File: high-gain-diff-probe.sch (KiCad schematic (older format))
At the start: 51 parts

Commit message: Transformer driver?
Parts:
- added C13, C14, C? (x2): 100nF, symbol Device:C_Small
- added C? (x6): C, symbol Device:C
- added C? (x6): 47uF, symbol Device:CP1
- added D? (x4): D_Schottky, symbol Device:D_Schottky
- added J?: Barrel_Jack, symbol Connector:Barrel_Jack
- added L? (x2): 33uH, symbol Device:L
- added R?: 10k, symbol Device:R_US
- added T?: Transformer_SP_2S, symbol Device:Transformer_SP_2S
- added U?: L7815, symbol Regulator_Linear:L7815
- added U?: L7915, symbol Regulator_Linear:L7915
- added U?: SN6505ADBV, Package_TO_SOT_SMD:SOT-23-6, symbol Power_Management:SN6505ADBV
- added U?: LT3439, Package_SO:TSSOP-16-1EP_4.4x5mm_P0.65mm, symbol Regulator_Switching:LT3439
- gave numbers to parts that had none: 49
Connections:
- net labels added: +36V
- wire segments 146 -> 257
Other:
- note added: "TODO: Common\nmode trim"
- note added: "TODO: Gain trim"
- note added: "TODO: Or just 4 9V"
- moved on the sheet: C1, C10, C11, C12, C2, C3, C4, C5, C6, C7, C8, C9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

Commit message: Developing
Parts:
- removed C? (x4): C, symbol Device:C
- removed C? (x5): 47uF, symbol Device:CP1
- removed D? (x4): D_Schottky, symbol Device:D_Schottky
- removed FB1, FB2: Ferrite_Bead, symbol Device:Ferrite_Bead
- removed J?: Barrel_Jack, symbol Connector:Barrel_Jack
- removed L? (x2): 33uH, symbol Device:L
- removed R10: 6k, symbol Device:R_US
- removed R16, R18: 100, symbol Device:R_US
- removed R8: 316, symbol Device:R_US
- removed R?: 10k, symbol Device:R_US
- removed SW2: SW_Rotary2x6, symbol Switch:SW_Rotary2x6
- removed SW3: LOW PASS SELECT, symbol Switch:SW_SP3T
- removed SW4: EXTRA GAIN SELECT, symbol Switch:SW_SP3T
- removed T?: Transformer_SP_2S, symbol Device:Transformer_SP_2S
- removed U2: ADA4004-2, symbol Amplifier_Operational:ADA4075-2
- removed U3: ADA4000-2, symbol Amplifier_Operational:ADA4075-2
- removed U?: L7815, symbol Regulator_Linear:L7815
- removed U?: L7915, symbol Regulator_Linear:L7915
- removed U?: SN6505ADBV, Package_TO_SOT_SMD:SOT-23-6, symbol Power_Management:SN6505ADBV
- removed U?: LT3439, Package_SO:TSSOP-16-1EP_4.4x5mm_P0.65mm, symbol Regulator_Switching:LT3439
- added BT1, BT2, BT3, BT4: 9V, symbol Device:Battery_Cell
- added C21, C22: 100nF, symbol Device:C_Small
- added C24: 47uF, symbol Device:CP1
- added C25: 1uF, symbol Device:C
- added C5, C6: 27pF, symbol Device:C
- added C7, C8: 1-3pF, symbol Device:CTRIM
- added D6: LED, symbol Device:LED
- added D? (x2): 1N4001, Diode_THT:D_DO-41_SOD81_P10.16mm_Horizontal, symbol Diode:1N4001
- added J?: Conn_01x03_Female, symbol Connector:Conn_01x03_Female
- added R5, R6: 475k, symbol Device:R_US
- added RV1: 500, symbol Device:R_POT_US
- added SW2: ‎MRB24B‎, symbol Switch:SW_DP3T
- added SW3: SW_SPDT, symbol Switch:SW_SPDT
- added SW4: SW_DPST_x2, symbol Switch:SW_DPST_x2
- added SW5: SW_DP3T, symbol Switch:SW_DPST_x2
- added U2: ADA4004, Package_SO:SOIC-8_3.9x4.9mm_P1.27mm, symbol Amplifier_Operational:LMH6609MA
- added U3: BUF634A, Package_SO:SOIC-8-1EP_3.9x4.9mm_P1.27mm_EP2.41x3.81mm_ThermalVias, symbol high-gain-diff-probe:BUF634A
- C1: value 14pF -> 27pF
- C11: renamed from C7; value 12p -> 10p
- C12: renamed from C8; value 12p -> 10p
- C18: renamed from C10; value 33nF -> 120pF
- C2: renamed from C3; value 14pF -> 27pF
- C20: renamed from C12; value 330nF -> 33nF
- C26: renamed from C?; value C -> 1uF
- C27: renamed from C?; value C -> 100nF
- R1: value 950k -> 475k
- R14, R15: value 2.2k -> 10k
- R17: value 400 -> 15k
- R2: renamed from R3; value 950k -> 475k
- R7: renamed from R6; value 50k -> 47.5k
- R8: renamed from R5; value 50k -> 47.5k
- SW1: value SW_DP3T -> ‎MRB24B‎
- gave numbers to parts that had none: 3
- renumbered C6 to C10, C9 to C13, C13 to C16, C14 to C17, C11 to C19, C2 to C3, C5 to C9, R9 to R10, R19 to R16, R2 to R3, R7 to R9, RV1 to RV2
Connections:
- net labels removed: +36V, RG_1000X, RG_100X
- wire segments 257 -> 185
- no-connect marks 4 -> 3
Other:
- note added: "+-12.8V Offset Range"
- note removed: "TODO: Choose gain switch"
- note removed: "TODO: Common\nmode trim"
- note removed: "TODO: Gain trim"
- note removed: "TODO: LT1010\n"
- note removed: "TODO: Or just 4 9V"
- moved on the sheet: C1, C10, C14, C15, C16, C17, C18, C19, C2, C20, C23, C26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

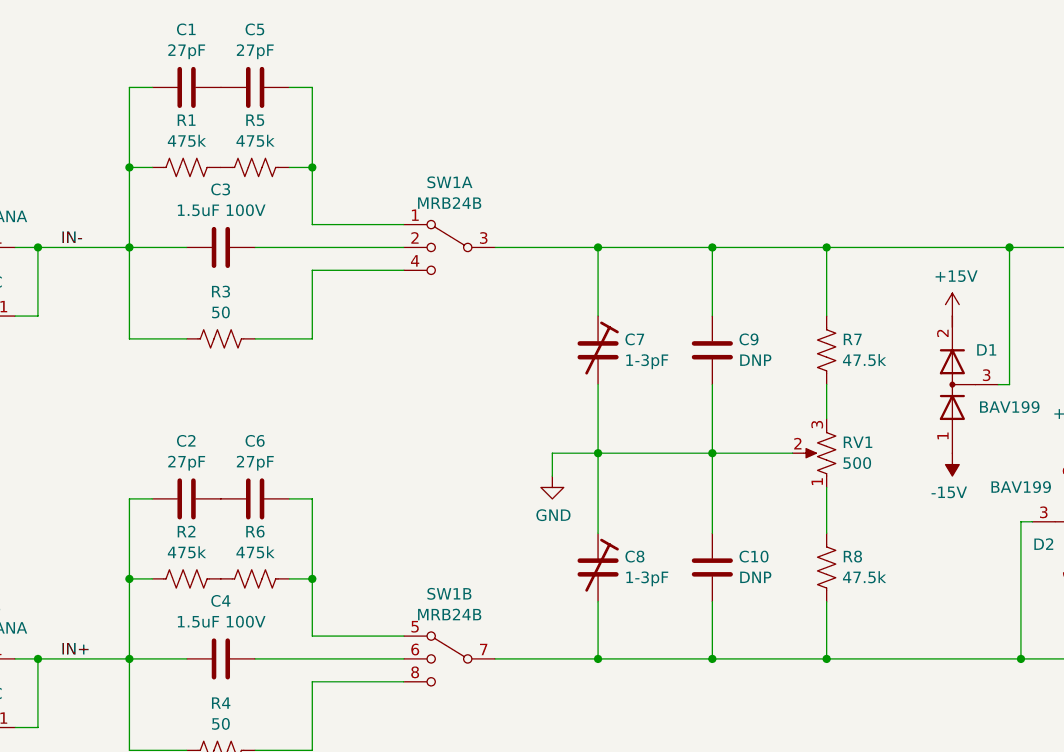
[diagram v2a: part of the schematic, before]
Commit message: Improve input divider ratio
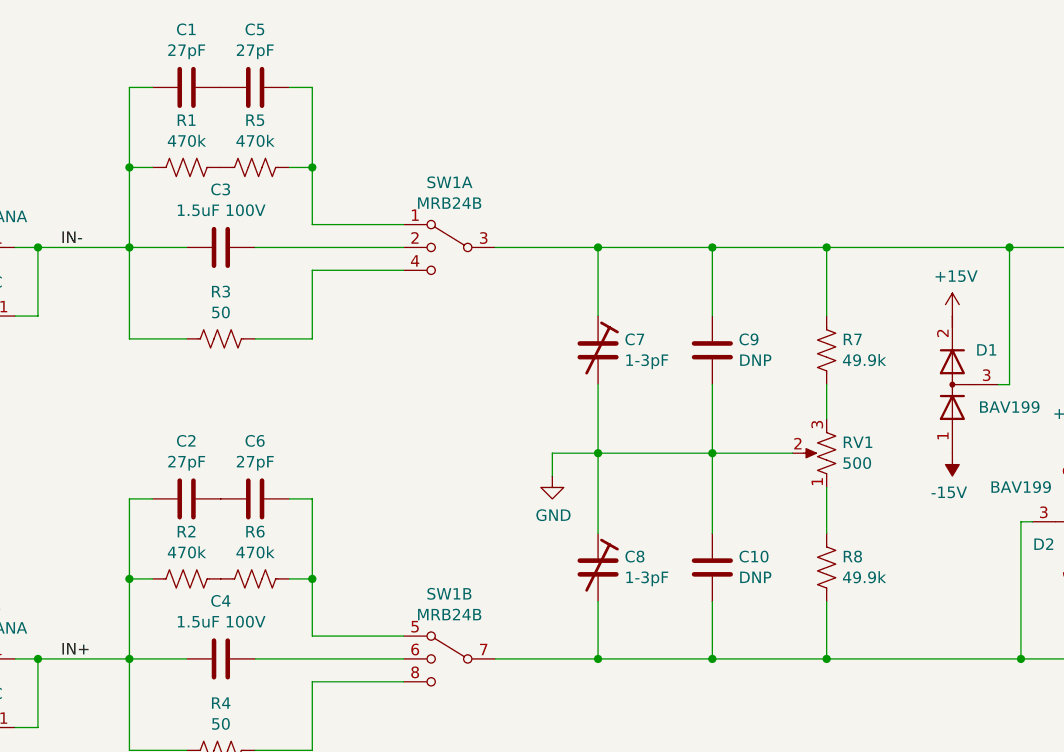
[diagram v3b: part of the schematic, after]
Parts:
- R1, R2, R5, R6: value 475k -> 470k
- R7, R8: value 47.5k -> 49.9k
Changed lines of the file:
@@
 P 5250 2350
 F 0 "R7" H 5318 2396 50  0000 L CNN
-F 1 "47.5k" H 5318 2305 50  0000 L CNN
+F 1 "49.9k" H 5318 2305 50  0000 L CNN
 F 2 "" V 5290 2340 50  0001 C CNN
 F 3 "~" H 5250 2350 50  0001 C CNN
@@
 P 5250 3300
 F 0 "R8" H 5318 3346 50  0000 L CNN
-F 1 "47.5k" H 5318 3255 50  0000 L CNN
+F 1 "49.9k" H 5318 3255 50  0000 L CNN
 F 2 "" V 5290 3290 50  0001 C CNN
 F 3 "~" H 5250 3300 50  0001 C CNN
@@
 P 2450 1550
 F 0 "R1" V 2245 1550 50  0000 C CNN
-F 1 "475k" V 2336 1550 50  0000 C CNN
+F 1 "470k" V 2336 1550 50  0000 C CNN
 F 2 "" V 2490 1540 50  0001 C CNN
 F 3 "~" H 2450 1550 50  0001 C CNN
@@
 P 2450 3350
 F 0 "R2" V 2245 3350 50  0000 C CNN
-F 1 "475k" V 2336 3350 50  0000 C CNN
+F 1 "470k" V 2336 3350 50  0000 C CNN
 F 2 "" V 2490 3340 50  0001 C CNN
 F 3 "~" H 2450 3350 50  0001 C CNN
@@
 Wire Wire Line
 	2200 2300 2450 2300
-Wire Wire Line
-	2750 2300 3000 2300
 $Comp
 L power:GND #PWR08
@@
 P 2750 3350
 F 0 "R6" V 2545 3350 50  0000 C CNN
-F 1 "475k" V 2636 3350 50  0000 C CNN
+F 1 "470k" V 2636 3350 50  0000 C CNN
 F 2 "" V 2790 3340 50  0001 C CNN
 F 3 "~" H 2750 3350 50  0001 C CNN
@@
 P 2750 1550
 F 0 "R5" V 2545 1550 50  0000 C CNN
-F 1 "475k" V 2636 1550 50  0000 C CNN
+F 1 "470k" V 2636 1550 50  0000 C CNN
 F 2 "" V 2790 1540 50  0001 C CNN
 F 3 "~" H 2750 1550 50  0001 C CNN
@@
 	0    1    1    0
 $EndComp
-Wire Wire Line
-	2900 1550 3000 1550
-Wire Wire Line
-	3000 1550 3000 1200
-Wire Wire Line
-	2900 1200 3000 1200
 $Comp
 L Device:C C1
@@
 	3800 1900 4250 1900
 Connection ~ 4250 1900
-Wire Wire Line
-	3000 2300 3000 2000
-Wire Wire Line
-	3000 2000 3400 2000
-Wire Wire Line
-	3400 1800 3000 1800
-Wire Wire Line
-	3000 1800 3000 1550
-Connection ~ 3000 1550
 $Comp
 L Switch:SW_DP3T SW2
@@
 Wire Wire Line
 	4300 8250 4850 8250
+Wire Wire Line
+	3000 2000 3400 2000
+Wire Wire Line
+	2750 2300 3000 2300
+Wire Wire Line
+	3000 2300 3000 2000
+Wire Wire Line
+	2900 1200 3000 1200
+Wire Wire Line
+	3000 1550 3000 1200
+Wire Wire Line
+	2900 1550 3000 1550
+Connection ~ 3000 1550
+Wire Wire Line
+	3400 1800 3000 1800
+Wire Wire Line
+	3000 1800 3000 1550
 $EndSCHEMATC

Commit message: Improve simulations
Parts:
- R1, R2, R5, R6: value 470k -> 475k
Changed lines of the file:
@@
 P 2450 1550
 F 0 "R1" V 2245 1550 50  0000 C CNN
-F 1 "470k" V 2336 1550 50  0000 C CNN
+F 1 "475k" V 2336 1550 50  0000 C CNN
 F 2 "" V 2490 1540 50  0001 C CNN
 F 3 "~" H 2450 1550 50  0001 C CNN
@@
 P 2450 3350
 F 0 "R2" V 2245 3350 50  0000 C CNN
-F 1 "470k" V 2336 3350 50  0000 C CNN
+F 1 "475k" V 2336 3350 50  0000 C CNN
 F 2 "" V 2490 3340 50  0001 C CNN
 F 3 "~" H 2450 3350 50  0001 C CNN
@@
 P 2750 3350
 F 0 "R6" V 2545 3350 50  0000 C CNN
-F 1 "470k" V 2636 3350 50  0000 C CNN
+F 1 "475k" V 2636 3350 50  0000 C CNN
 F 2 "" V 2790 3340 50  0001 C CNN
 F 3 "~" H 2750 3350 50  0001 C CNN
@@
 P 2750 1550
 F 0 "R5" V 2545 1550 50  0000 C CNN
-F 1 "470k" V 2636 1550 50  0000 C CNN
+F 1 "475k" V 2636 1550 50  0000 C CNN
 F 2 "" V 2790 1540 50  0001 C CNN
 F 3 "~" H 2750 1550 50  0001 C CNN

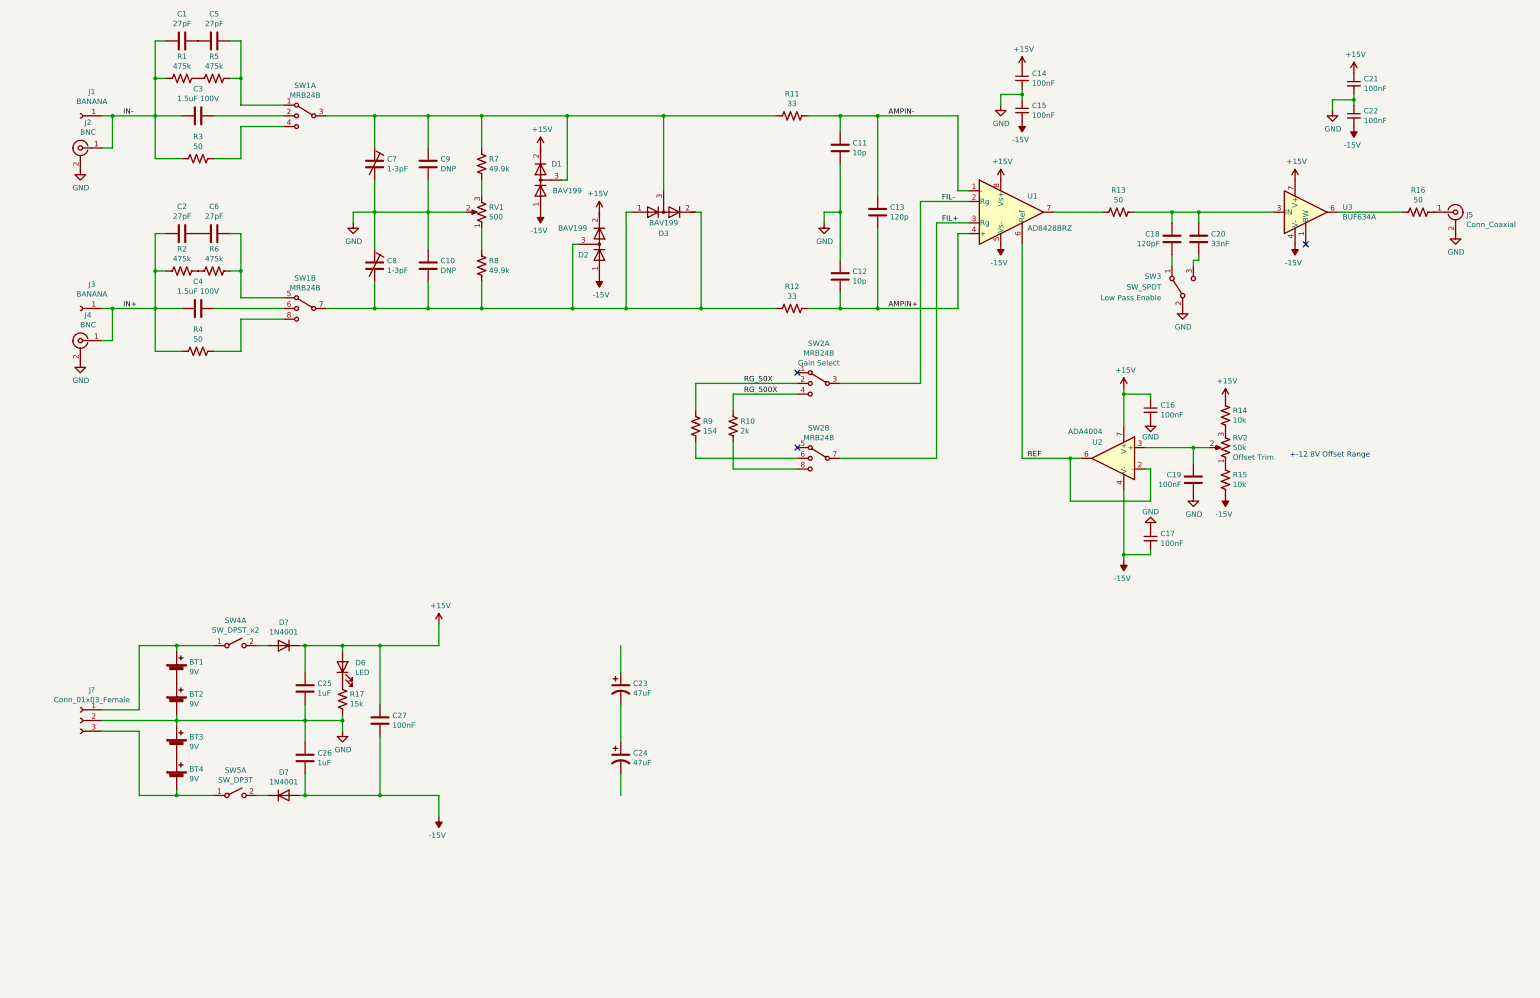
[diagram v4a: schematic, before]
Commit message: Implement capacitance multiplier, power overvoltage protection, and signal out of range comparators
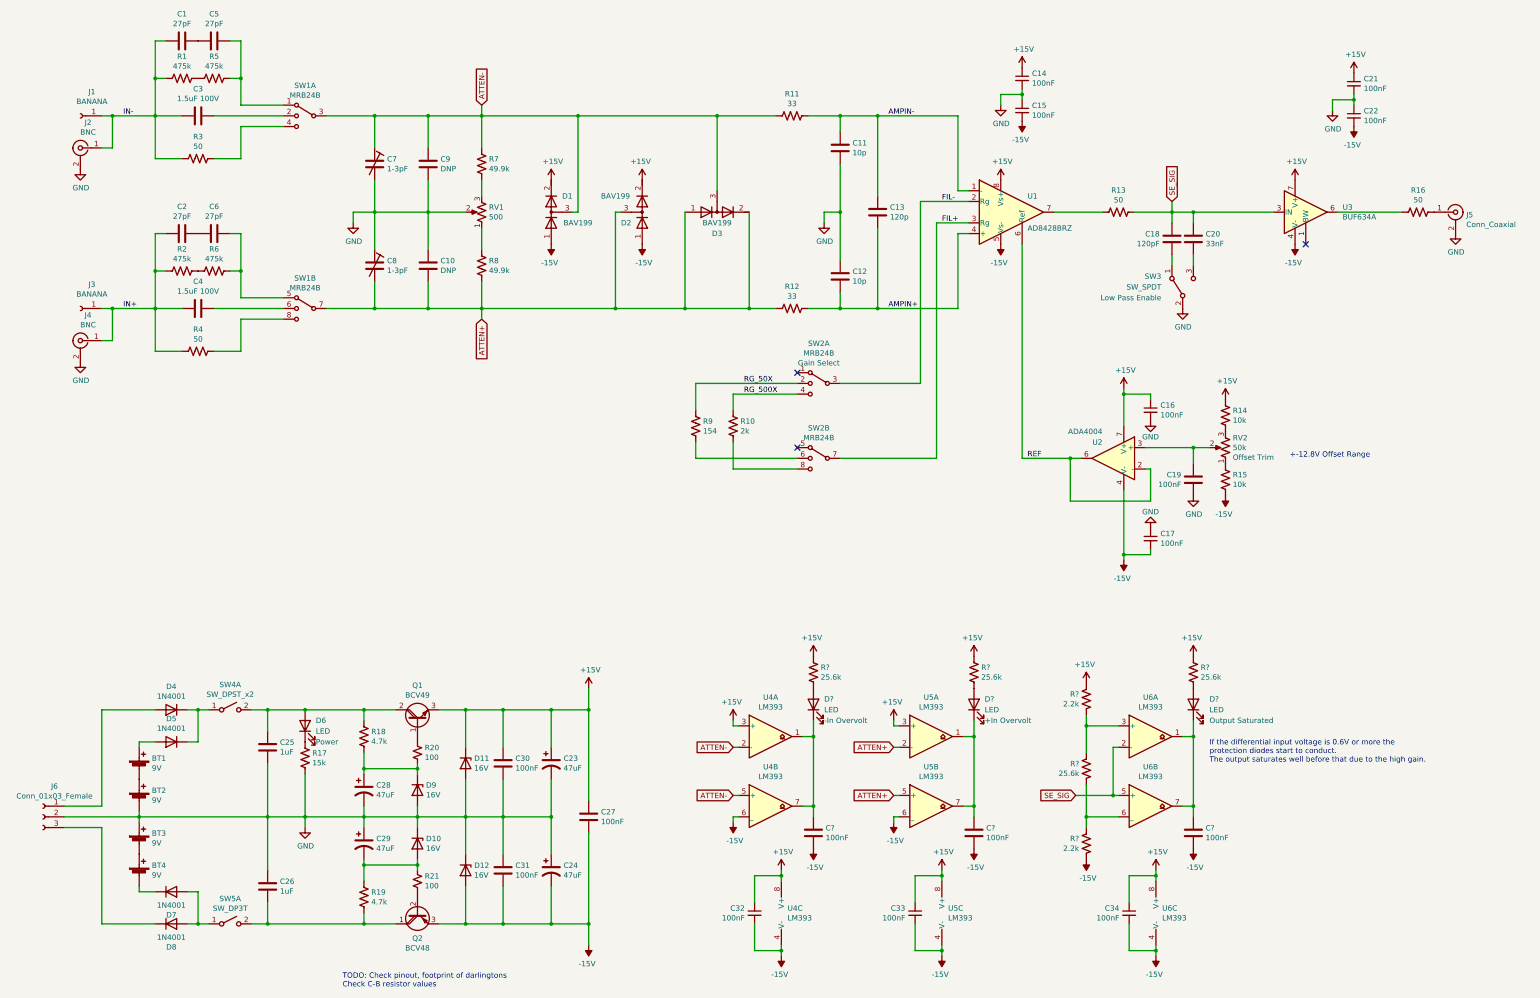
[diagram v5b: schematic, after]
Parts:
- added C28, C29: 47uF, symbol Device:CP1
- added C30, C31, C? (x3): 100nF, symbol Device:C
- added C32, C33, C34: 100nF, symbol Device:C_Small
- added D10, D11, D12, D9: 16V, Diode_SMD:D_SMF, symbol Diode:BZD27Cxx
- added D4, D8: 1N4001, Diode_THT:D_DO-41_SOD81_P10.16mm_Horizontal, symbol Diode:1N4001
- added D? (x3): LED, symbol Device:LED
- added Q1: BCV49, Package_TO_SOT_SMD:SOT-89-3_Handsoldering, symbol Transistor_BJT:BCV49
- added Q2: BCV48, Package_TO_SOT_SMD:SOT-89-3_Handsoldering, symbol Transistor_BJT:BC516
- added R18, R19: 4.7k, symbol Device:R_US
- added R20, R21: 100, symbol Device:R_Small_US
- added R? (x2): 2.2k, symbol Device:R_US
- added R? (x4): 25.6k, symbol Device:R_US
- added U4, U5, U6: LM393, symbol Comparator:LM393
- D6: Name (none) -> Power
- gave numbers to parts that had none: 3
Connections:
- net +15V: now also C23.1, C30.1, C32.1, C33.1, C34.1, D11.1 (K), Q1.3 (E), R?.2, R?.2, R?.2, R?.2, U4.3 (+), U4.8 (V+), U5.3 (+), U5.8 (V+), U6.8 (V+); no longer C25.1, D5.1 (K), D6.2 (A)
- net -15V: now also C24.2, C31.2, C32.2, C33.2, C34.2, C?.1, C?.1, C?.1, D12.2 (A), Q2.3 (E), R?.1, U4.4 (V-), U4.6 (_), U5.4 (V-), U5.6 (_), U6.4 (V-); no longer C26.2, D7.2 (A)
- net GND: now also C23.2, C24.1, C28.2, C29.1, C30.2, C31.1, D10.1 (K), D11.2 (A), D12.1 (K), D9.2 (A)
- net SE_SIG: now reaches C18.1, C20.1, R13.1, U3.3 (IN)
- net SE_SIG: now also U6.2 (-), U6.5 (+)
- net ATTEN+: now reaches C10.2, C8.2, D2.3 (common), D3.1 (A), D3.2 (K), R12.2, R8.2, SW1.7
- net ATTEN+: now also U5.2 (-), U5.5 (+)
- net ATTEN-: now reaches C7.1, C9.1, D1.3 (common), D3.3 (common), R11.2, R7.1, SW1.3
- net ATTEN-: now also U4.2 (-), U4.5 (+)
- net at D5.2 (A): now also BT1.1 (+); no longer SW4.2 (B)
- net at D7.1 (K): now also BT4.2 (-); no longer SW5.2 (B)
- new net: D8.1 (K), J6.3 (Pin_3)
- new net: D7.2 (A), D8.2 (A), SW5.1 (A)
- new net: D4.1 (K), D5.1 (K), SW4.1 (A)
- new net: D4.2 (A), J6.1 (Pin_1)
- new net: C26.2, Q2.1 (C), R19.2, SW5.2 (B)
- new net: Q2.2 (B), R21.2
- new net: C29.2, D10.2 (A), R19.1, R21.1
- new net: C25.1, D6.2 (A), Q1.2 (C), R18.1, SW4.2 (B)
- new net: C28.1, D9.1 (K), R18.2, R20.2
- new net: Q1.1 (B), R20.1
- new net: C?.2, D?.1 (K), U4.1, U4.7
- new net: C?.2, D?.1 (K), U5.1, U5.7
- new net: C?.2, D?.1 (K), U6.1, U6.7
- new net: R?.1, R?.2, U6.3 (+)
- new net: R?.1, R?.2, U6.6 (_)
- new net: D?.2 (A), R?.1 (x3)
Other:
- note added: "If the differential input voltage is 0.6V or more the\nprotection diodes start to conduct.\nThe output saturates well before that due to the high gain."
- note added: "TODO: Check pinout, footprint of darlingtons\nCheck C-B resistor values"
- moved on the sheet: BT1, BT2, BT3, BT4, C20, C23, C24, C25, C26, C27, D1, D2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
